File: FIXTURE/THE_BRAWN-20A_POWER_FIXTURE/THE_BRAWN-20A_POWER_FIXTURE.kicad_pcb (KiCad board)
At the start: 2 copper layers, 100 x 100 mm, 71 parts, among them J1 Pins_2.54_1x3, J10 Pins_2.54_1x2, J2 Pins_2.54_1x3, J3 Pins_2.54_1x4, J4 Pins_2.54_1x3, J5 Pins_2.54_1x2, J6 Pins_2.54_1x3, J7 Pins_2.54_1x4, J8 Pins_2.54_1x3, J9 Pins_2.54_1x3, M1 Mount_M3, M10 Mount_M3, M11 Mount_M3, M12 Mount_M3, M13 Mount_M3, M14 Mount_M3, M15 Mount_M3, M16 Mount_M3, M17 Mount_M3, M18 Mount_M3, M2 Mount_M3, M21 Mount_M3, M22 Mount_M3, M3 Mount_M3, M4 Mount_M3, M5 Mount_M3, M6 Mount_M3, M7 Mount_M3, M8 Mount_M3, M9 Mount_M3

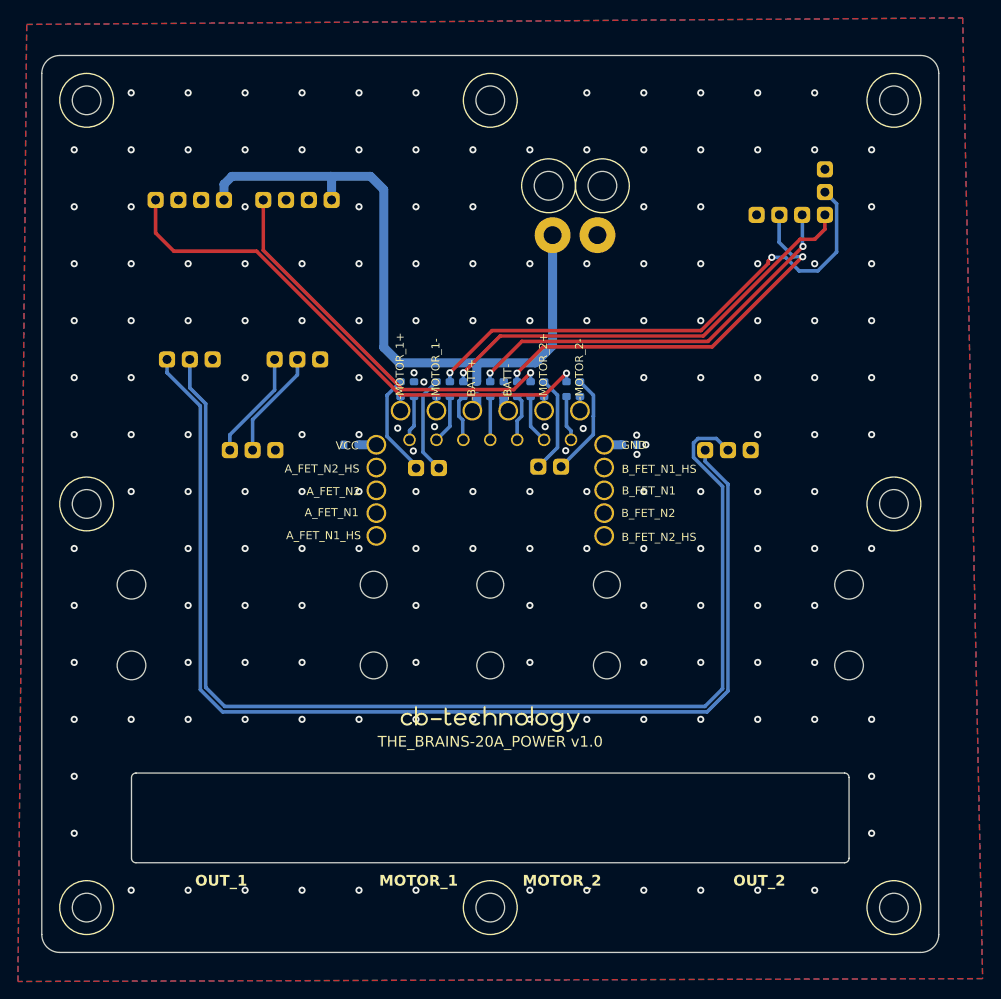
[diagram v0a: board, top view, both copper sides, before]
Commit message: Finish Tracking Power Fixture PCB
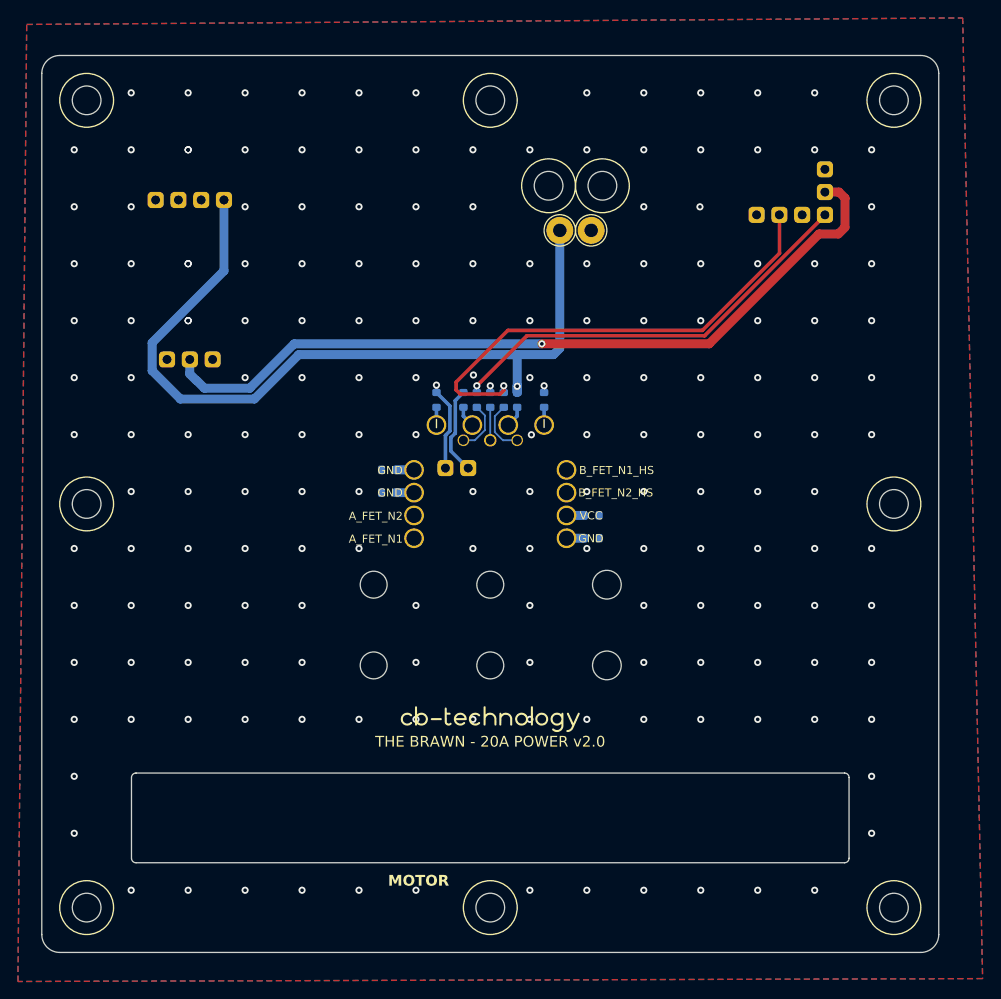
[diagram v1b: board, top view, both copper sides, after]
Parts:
- removed J10: Pins_2.54_1x2, .J_Connector:Pins-2.54-1x2
- removed J6, J8, J9: Pins_2.54_1x3, .J_Connector:Pins-2.54-1x3
- removed J7: Pins_2.54_1x4, .J_Connector:Pins-2.54-1x4
- removed M17, M18, M21, M22: Mount_M3, .M_Mechanical:Mount_M3
- removed R12, R13, R18, R19, R5, R6: 0R, .R_Resistor:R_0603
- removed the TP1 at (207.3, 133.4)
- removed TP14, TP15, TP23, TP25, TP26, TP27, TP30, TP31, TP8: TestPoint, TestPoint:TestPoint_THTPad_D3.0mm_Drill1.5mm
- added R14: 0R, .R_Resistor:R_0603, B.Cu at (231.3, 141.3)
- added R15: 0R, .R_Resistor:R_0603, B.Cu at (231.3, 143.8)
- added TP16: TestPoint, TestPoint:TestPoint_THTPad_D3.0mm_Drill1.5mm, F.Cu at (227.8, 109.5)
- added TP17: TestPoint, TestPoint:TestPoint_THTPad_D3.0mm_Drill1.5mm, F.Cu at (231.2, 109.5)
- J4: moved to B.Cu
- M1, M2, M3, M4, M5, M6, M7, M8: footprint .M_Mechanical:Mount_M3 -> M_Mechanical:Mount_M3
- moved M15 53.0 mm to (233.0, 149.0)
- moved M16 53.0 mm to (233.0, 158.0)
- moved M14 27.5 mm to (207.0, 158.0)
- moved R2 12.7 mm to (208.7, 138.7), turned to 0 degrees
- moved J4 12.3 mm to (189.0, 123.9), turned to 90 degrees
- moved TP13 12.0 mm to (223.0, 132.9)
- moved J3 12.0 mm to (190.3, 106.1)
- moved J5 10.4 mm to (215.0, 136.0)
- moved R1 9.09 mm to (208.7, 136.2), turned to 0 degrees
- moved R4 7.60 mm to (214.0, 128.4)
- moved R10 6.12 mm to (226.0, 128.4)
- moved R9 6.12 mm to (223.0, 128.4)
- moved R7 5.63 mm to (217.0, 128.4)
- moved R8 4.66 mm to (220.0, 128.4)
- moved TP19 4.21 mm to (228.5, 138.7)
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- renumbered TP2 to TP1, TP19 to TP10, TP22 to TP11, TP24 to TP12, TP9 to TP18, TP10 to TP19, TP3 to TP2, TP12 to TP20, TP20 to TP21, TP4 to TP3, TP21 to TP4, TP17 to TP5, TP16 to TP6, TP18 to TP7
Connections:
- J2 pad 1: /SIGNAL2 -> unconnected-(J2-Pad1)
- J3 pad 4: /OUT1 -> /SERVO
- J4 pad 2: /5V0_S1 -> /5V0
- J4 pad 3: /OUT1_S -> /SERVO_OUT
- J5 pad 1: /MOTOR_2+ -> /MOTOR_1+
- J5 pad 2: /MOTOR_2- -> /MOTOR_1-
- R1 pad 1: Net-(R1-Pad1) -> /GND
- R1 pad 2: /MOTOR_1+ -> Net-(R1-Pad2)
- R10 pad 2: /SIGNAL2 -> /GND
- R2 pad 1: Net-(R2-Pad1) -> /GND
- R2 pad 2: /MOTOR_1- -> Net-(R2-Pad2)
- R3 pad 2: /BATT+ -> /SIGNAL1
- R4 pad 2: /GND -> /MOTOR_1+
- R7 pad 2: /GND -> /MOTOR_1-
- R8 pad 2: /5V0 -> /GND
- R9 pad 2: /SIGNAL1 -> /BATT+
- TP1 pad 1: /A_FET_N2_HS -> Net-(R1-Pad2)
- TP10 pad 1: Net-(R10-Pad1) -> Net-(R8-Pad1)
- TP11 pad 1: Net-(R4-Pad1) -> Net-(R9-Pad1)
- TP12 pad 1: Net-(R5-Pad1) -> Net-(R10-Pad1)
- TP13 pad 1: Net-(R7-Pad1) -> Net-(R11-Pad1)
- TP19 pad 1: /B_FET_N1 -> /B_FET_N2_HS
- TP2 pad 1: /A_FET_N2 -> Net-(R2-Pad2)
- TP20 pad 1: /B_FET_N2 -> Net-(R14-Pad1)
- TP21 pad 1: /B_FET_N2_HS -> Net-(R15-Pad1)
- TP3 pad 1: /A_FET_N1 -> /A_FET_N2
- TP4 pad 1: /A_FET_N1_HS -> /A_FET_N1
- TP5 pad 1: Net-(R9-Pad1) -> Net-(R3-Pad1)
- TP6 pad 1: Net-(R2-Pad1) -> Net-(R4-Pad1)
- TP7 pad 1: Net-(R3-Pad1) -> Net-(R7-Pad1)
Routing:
- net /5V0_S2: track 129.9 -> 0.00 mm
- net /OUT2_S: track 127.1 -> 0.00 mm
- net /OUT2: track 59.0 -> 0.00 mm, vias 1 -> 0
- net /SIGNAL2: track 45.3 -> 0.00 mm, vias 2 -> 0
- net /OUT1: track 43.6 -> 0.00 mm, vias 1 -> 0
- net /5V0: track 58.3 -> 88.5 mm, vias 2 -> 1
- net /BATT+: track 75.5 -> 91.5 mm, vias 0 -> 1
- net /OUT1_S: track 12.2 -> 0.00 mm
- net /5V0_S1: track 12.2 -> 0.00 mm
- net /MOTOR_2-: track 11.6 -> 0.00 mm
- net /MOTOR_2+: track 11.0 -> 0.00 mm
- net /INVERT: track 44.6 -> 54.3 mm, vias 2 -> 1
- net Net-(R12-Pad1): track 5.45 -> 0.00 mm
- net Net-(R13-Pad1): track 5.04 -> 0.00 mm
- net Net-(R3-Pad1): track 1.78 -> 5.79 mm
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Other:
- board text added: "MOTOR"
- board text added: "SERVO/BEC"
- board text added: "THE BRAWN - 20A POWER v2.0"
- board text removed: "-BATT+"
- board text removed: "-BATT-"
- board text removed: "-MOTOR_1+"
- board text removed: "-MOTOR_1-"
- board text removed: "-MOTOR_2+"
- board text removed: "-MOTOR_2-"
- board text removed: "A_FET_N1_HS"
- board text removed: "A_FET_N2_HS"
- board text removed: "B_FET_N1"
- board text removed: "B_FET_N2"
- board text removed: "MOTOR_1"
- board text removed: "MOTOR_2"
- board text removed: "OUT_1"
- board text removed: "OUT_2"
- board text removed: "S1"
- board text removed: "S2"
- board text removed: "SERVO1"
- board text removed: "SERVO2"
- board text removed: "THE_BRAINS-20A_POWER v1.0"
